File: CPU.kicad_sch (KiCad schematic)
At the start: 215 parts, among them J1 Conn_02x36_Top_Bottom, P10 Conn_02x08_Counter_Clockwise, P2 Conn_02x13_Top_Bottom, P3 Conn_02x13_Top_Bottom, P4 Conn_02x08_Counter_Clockwise, P5 Conn_02x25_Counter_Clockwise, P6 Conn_02x25_Counter_Clockwise, P7 Conn_02x07_Counter_Clockwise, P8 Conn_02x08_Counter_Clockwise

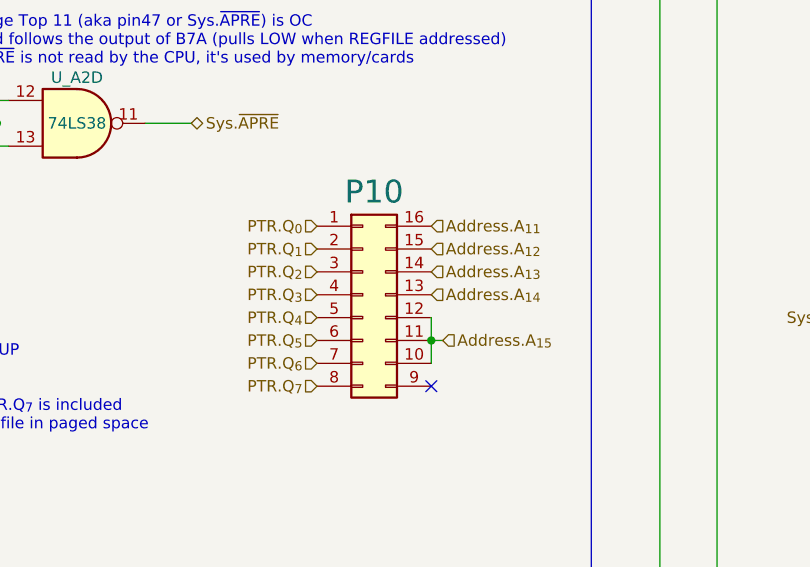
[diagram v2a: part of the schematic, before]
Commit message: Remove P10
This diagnostics connector gives direct access to page table DRAM, we don't need
it. In fact it could have been located in B row with much shorter traces, but
the only available position there is occupied by second ISA ROM half.
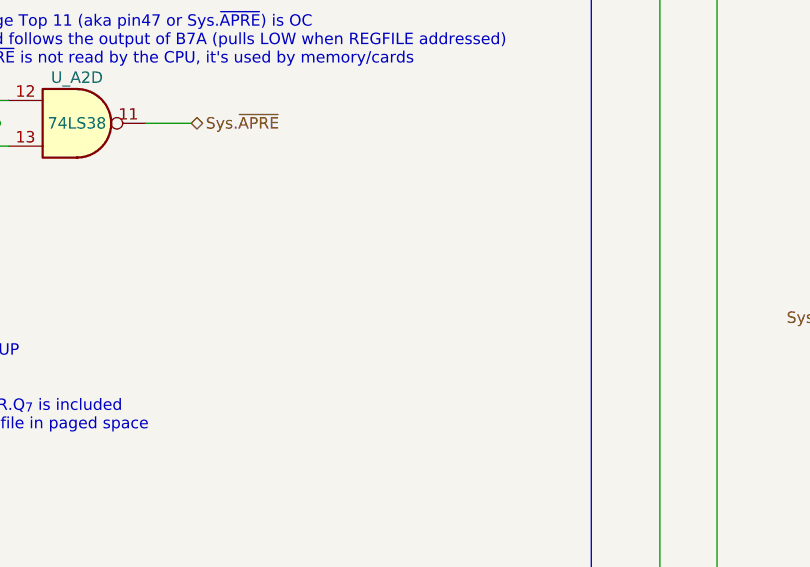
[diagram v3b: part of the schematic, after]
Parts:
- removed P10: Conn_02x08_Counter_Clockwise, Package_DIP:DIP-16_W7.62mm_Socket, symbol Connector_Generic:Conn_02x08_Counter_Clockwise
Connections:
- no-connect marks 94 -> 93
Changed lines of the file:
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@@
   (junction (at 107.95 429.26) (diameter 0) (color 0 0 0 0)
   )
-  (junction (at 341.63 494.03) (diameter 0) (color 0 0 0 0)
-  )
   (junction (at 144.78 457.2) (diameter 0) (color 0 0 0 0)
   )
@@
   (no_connect (at 440.69 746.76))
   (no_connect (at 289.56 142.24))
-  (no_connect (at 341.63 499.11))
   (no_connect (at 386.08 356.87))
   (no_connect (at 521.97 367.03))
@@
     (stroke (width 0) (type default) (color 189 121 184 1))
   )
-  (wire (pts (xy 341.63 491.49) (xy 341.63 494.03))
-    (stroke (width 0) (type default) (color 0 0 0 0))
-  )
   (wire (pts (xy 871.22 123.19) (xy 875.03 123.19))
     (stroke (width 0) (type default) (color 0 0 0 0))
@@
     (stroke (width 0) (type default) (color 0 0 0 0))
   )
-  (wire (pts (xy 341.63 494.03) (xy 341.63 496.57))
-    (stroke (width 0) (type default) (color 0 0 0 0))
-  )
   (wire (pts (xy 615.95 748.03) (xy 615.95 758.19))
     (stroke (width 0) (type default) (color 0 0 0 0))
@@
     (stroke (width 0) (type default) (color 0 0 0 0))
   )
-  (wire (pts (xy 342.9 494.03) (xy 341.63 494.03))
-    (stroke (width 0) (type default) (color 0 0 0 0))
-  )
   (wire (pts (xy 864.87 245.11) (xy 886.46 245.11))
     (stroke (width 0) (type default) (color 0 0 0 0))
@@
     (effects (font (size 1.27 1.27)) (justify right))
   )
-  (hierarchical_label "PTR.Q_{7}" (shape input) (at 328.93 499.11 180)
-    (effects (font (size 1.27 1.27)) (justify right))
-  )
   (hierarchical_label "~{M13_EN}" (shape output) (at 674.37 142.24 0)
     (effects (font (size 1.27 1.27)) (justify left))
@@
     (effects (font (size 1.27 1.27)) (justify right))
   )
-  (hierarchical_label "Address.A_{15}" (shape input) (at 342.9 494.03 0)
-    (effects (font (size 1.27 1.27)) (justify left))
-  )
   (hierarchical_label "CondRegOrPageOut" (shape output) (at 300.99 454.66 0)
     (effects (font (size 1.27 1.27)) (justify left))
@@
     (effects (font (size 1.27 1.27)) (justify right))
   )
-  (hierarchical_label "Address.A_{14}" (shape input) (at 341.63 488.95 0)
-    (effects (font (size 1.27 1.27)) (justify left))
-  )
   (hierarchical_label "~{M13_EN}" (shape input) (at 985.52 270.51 180)
     (effects (font (size 1.27 1.27)) (justify right))
@@
     (effects (font (size 1.27 1.27)) (justify left))
   )
-  (hierarchical_label "PTR.Q_{6}" (shape input) (at 328.93 496.57 180)
-    (effects (font (size 1.27 1.27)) (justify right))
-  )
   (hierarchical_label "~{AddrMToData}" (shape input) (at 109.22 472.44 180)
     (effects (font (size 1.27 1.27)) (justify right))
@@
     (effects (font (size 1.27 1.27)) (justify left))
   )
-  (hierarchical_label "Address.A_{13}" (shape input) (at 341.63 486.41 0)
-    (effects (font (size 1.27 1.27)) (justify left))
-  )
   (hierarchical_label "DMA.~{INTRequest}" (shape input) (at 909.32 250.19 180)
     (effects (font (size 1.27 1.27)) (justify right))
@@
     (effects (font (size 1.27 1.27)) (justify left))
   )
-  (hierarchical_label "Address.A_{12}" (shape input) (at 341.63 483.87 0)
-    (effects (font (size 1.27 1.27)) (justify left))
-  )
   (hierarchical_label "~{WorkAddr_LD_LO}" (shape output) (at 674.37 152.4 0)
     (effects (font (size 1.27 1.27)) (justify left))
@@
     (effects (font (size 1.27 1.27)) (justify left))
   )
-  (hierarchical_label "PTR.Q_{1}" (shape input) (at 328.93 483.87 180)
-    (effects (font (size 1.27 1.27)) (justify right))
-  )
   (hierarchical_label "Sys.~{A_{9}}" (shape bidirectional) (at 41.91 408.94 180)
     (effects (font (size 1.27 1.27)) (justify right))
@@
     (effects (font (size 1.27 1.27)) (justify right))
   )
-  (hierarchical_label "Address.A_{11}" (shape input) (at 341.63 481.33 0)
-    (effects (font (size 1.27 1.27)) (justify left))
-  )
   (hierarchical_label "MWR.A6_{3}" (shape input) (at 740.41 798.83 90)
     (effects (font (size 1.27 1.27)) (justify left))
@@
     (effects (font (size 1.27 1.27)) (justify left))
   )
-  (hierarchical_label "PTR.Q_{2}" (shape input) (at 328.93 486.41 180)
-    (effects (font (size 1.27 1.27)) (justify right))
-  )
   (hierarchical_label "~{Swap_OE}" (shape output) (at 466.09 623.57 0)
     (effects (font (size 1.27 1.27)) (justify left))
@@
     (effects (font (size 1.27 1.27)) (justify right))
   )
-  (hierarchical_label "PTR.Q_{5}" (shape input) (at 328.93 494.03 180)
-    (effects (font (size 1.27 1.27)) (justify right))
-  )
   (hierarchical_label "MWR.F1_{5}" (shape input) (at 618.49 798.83 90)
     (effects (font (size 1.27 1.27)) (justify left))
@@
     (effects (font (size 1.27 1.27)) (justify left))
   )
-  (hierarchical_label "PTR.Q_{0}" (shape input) (at 328.93 481.33 180)
-    (effects (font (size 1.27 1.27)) (justify right))
-  )
   (hierarchical_label "Sys.~{INTREQ}" (shape input) (at 720.09 101.6 180)
     (effects (font (size 1.27 1.27)) (justify right))
@@
     (effects (font (size 1.27 1.27)) (justify left))
   )
-  (hierarchical_label "PTR.Q_{4}" (shape input) (at 328.93 491.49 180)
-    (effects (font (size 1.27 1.27)) (justify right))
-  )
   (hierarchical_label "M10C_a" (shape output) (at 450.85 262.89 0)
     (effects (font (size 1.27 1.27)) (justify left))
@@
     (effects (font (size 1.27 1.27)) (justify right))
   )
-  (hierarchical_label "PTR.Q_{3}" (shape input) (at 328.93 488.95 180)
-    (effects (font (size 1.27 1.27)) (justify right))
-  )
   (hierarchical_label "Sys.~{CPL_{2}}" (shape bidirectional) (at 100.33 397.51 180)
     (effects (font (size 1.27 1.27)) (justify right))
@@
     (pin "9")
   )
-  (symbol (lib_id "Connector_Generic:Conn_02x08_Counter_Clockwise") (at 334.01 488.95 0) (unit 1)
-    (in_bom yes) (on_board yes)
-    (property "Reference" "P10" (id 0) (at 335.28 477.52 0)
-      (effects (font (size 2.54 2.54)))
-    )
-    (property "Value" "Conn_02x08_Counter_Clockwise" (id 1) (at 335.28 477.52 0)
-      (effects (font (size 1.27 1.27)) hide)
-    )
-    (property "Footprint" "Package_DIP:DIP-16_W7.62mm_Socket" (id 2) (at 334.01 488.95 0)
-      (effects (font (size 1.27 1.27)) hide)
-    )
-    (property "Datasheet" "~" (id 3) (at 334.01 488.95 0)
-      (effects (font (size 1.27 1.27)) hide)
-    )
-    (pin "1")
-    (pin "10")
-    (pin "11")
-    (pin "12")
-    (pin "13")
-    (pin "14")
-    (pin "15")
-    (pin "16")
-    (pin "2")
-    (pin "3")
-    (pin "4")
-    (pin "5")
-    (pin "6")
-    (pin "7")
-    (pin "8")
-    (pin "9")
-  )
   (symbol (lib_id "74xx:74LS74") (at 684.53 41.91 0) (unit 3)
     (in_bom yes) (on_board yes)
@@
       (reference "P8") (unit 1) (value "Conn_02x08_Counter_Clockwise") (footprint "Package_DIP:DIP-16_W7.62mm_Socket")
     )
-    (path "/5526b978-6091-4308-8cc5-df61e46dff5e"
-      (reference "P10") (unit 1) (value "Conn_02x08_Counter_Clockwise") (footprint "Package_DIP:DIP-16_W7.62mm_Socket")
-    )
     (path "/314bd753-a531-42e2-88ae-163e7747a0c2"

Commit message: Fixed U13H/U13L footprint
Noticed in time and replaced with proper DIP16 instead of DIP20, erroneously
left over from the original ROM
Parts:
- U_BH13, U_BL13: footprint Package_DIP:DIP-20_W7.62mm -> Package_DIP:DIP-16_W7.62mm
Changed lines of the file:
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@@
     )
     (property "Value" "93427C" (id 1) (at 224.79 54.61 90))
-    (property "Footprint" "Package_DIP:DIP-20_W7.62mm" (id 2) (at 247.65 29.21 0)
+    (property "Footprint" "Package_DIP:DIP-16_W7.62mm" (id 2) (at 247.65 29.21 0)
       (effects (font (size 1.27 1.27)) hide)
     )
@@
     )
     (property "Value" "93427C" (id 1) (at 224.79 97.79 90))
-    (property "Footprint" "Package_DIP:DIP-20_W7.62mm" (id 2) (at 247.65 72.39 0)
+    (property "Footprint" "Package_DIP:DIP-16_W7.62mm" (id 2) (at 247.65 72.39 0)
       (effects (font (size 1.27 1.27)) hide)
     )
@@
     )
     (path "/c0266c95-ae17-45e2-bf80-9f2f693576d4"
-      (reference "U_BH13") (unit 1) (value "93427C") (footprint "Package_DIP:DIP-20_W7.62mm")
+      (reference "U_BH13") (unit 1) (value "93427C") (footprint "Package_DIP:DIP-16_W7.62mm")
     )
     (path "/87f1dd62-191b-408d-8ad7-44a75dff6333"
-      (reference "U_BL13") (unit 1) (value "93427C") (footprint "Package_DIP:DIP-20_W7.62mm")
+      (reference "U_BL13") (unit 1) (value "93427C") (footprint "Package_DIP:DIP-16_W7.62mm")
     )
     (path "/8af415d4-268f-42b0-9c51-01a0acd645d3"

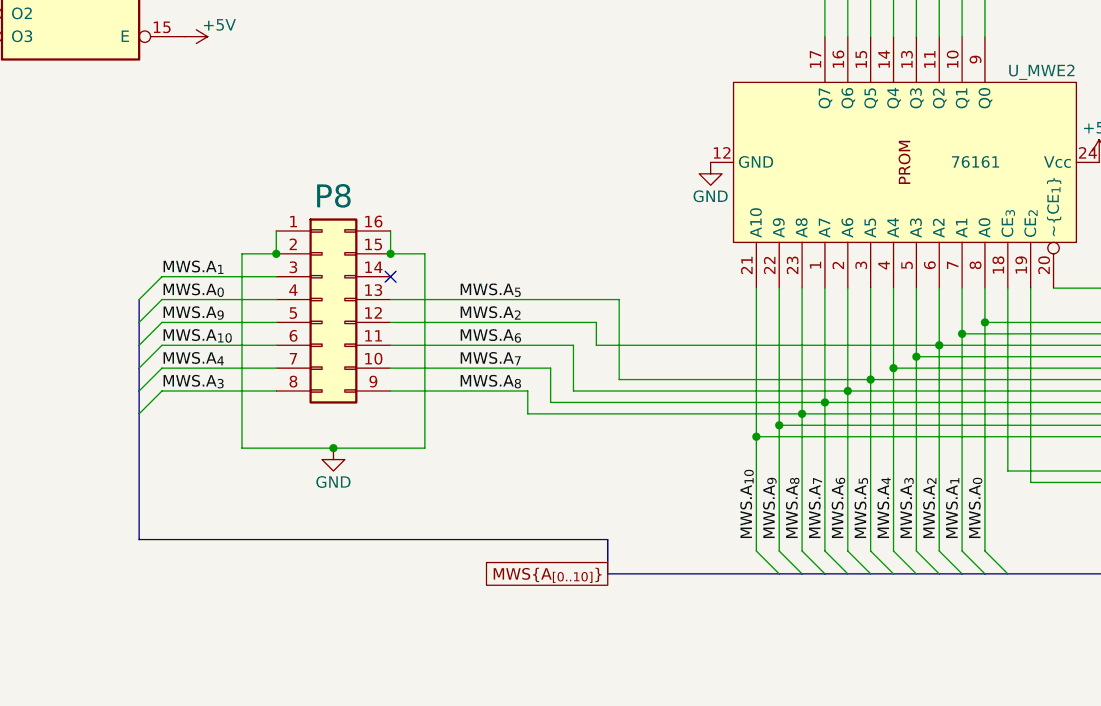
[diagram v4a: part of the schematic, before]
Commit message: P8 pins reassigned
Change connector type to IDC for smaller footprint and rearrange pins so that
less vias are needed.

All the footprints brought in sync with the PCB
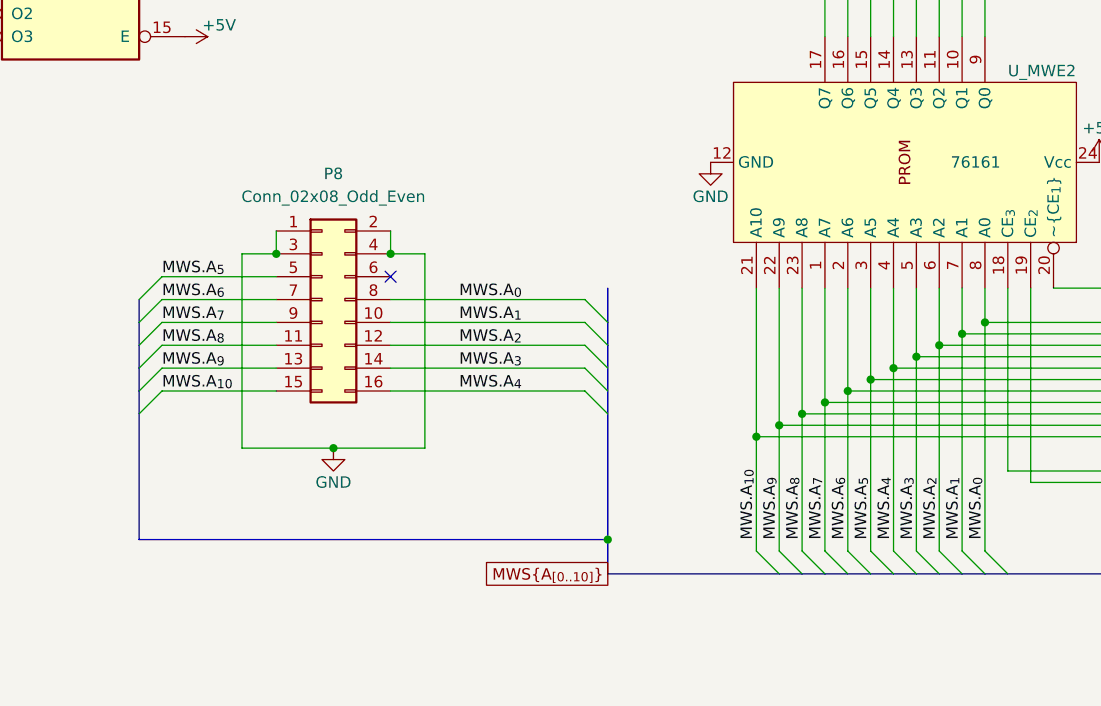
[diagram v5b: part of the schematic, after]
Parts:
- removed P8: Conn_02x08_Counter_Clockwise, Package_DIP:DIP-16_W7.62mm_Socket, symbol Connector_Generic:Conn_02x08_Counter_Clockwise
- added P8: Conn_02x08_Odd_Even, Connector_IDC:IDC-Header_2x08_P2.54mm_Vertical, symbol Connector_Generic:Conn_02x08_Odd_Even
- C31, C32, C33, C34, C35: footprint Capacitor_THT:C_Disc_D4.3mm_W1.9mm_P5.00mm -> Capacitor_THT:C_Rect_L9.0mm_W2.5mm_P7.50mm_MKT
- C52, C53: footprint Capacitor_THT:CP_Axial_L25.0mm_D10.0mm_P30.00mm_Horizontal -> Capacitor_THT:CP_Radial_D8.0mm_P3.50mm
- R18: footprint Resistor_THT:R_Axial_DIN0207_L6.3mm_D2.5mm_P10.16mm_Horizontal -> Resistor_THT:R_Axial_DIN0207_L6.3mm_D2.5mm_P7.62mm_Horizontal
- R19: footprint Resistor_THT:R_Axial_DIN0207_L6.3mm_D2.5mm_P10.16mm_Horizontal -> Resistor_THT:R_Axial_DIN0204_L3.6mm_D1.6mm_P7.62mm_Horizontal
- R22, R23: footprint Resistor_THT:R_Axial_DIN0204_L3.6mm_D1.6mm_P2.54mm_Vertical -> Resistor_THT:R_Axial_DIN0204_L3.6mm_D1.6mm_P5.08mm_Horizontal
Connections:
- net GND: now also P8.1 (Pin_1), P8.2 (Pin_2), P8.3 (Pin_3), P8.4 (Pin_4)
- net MWS.A_{0}: now also P8.8 (Pin_8)
- net MWS.A_{10}: now also P8.15 (Pin_15)
- net MWS.A_{1}: now also P8.10 (Pin_10)
- net MWS.A_{2}: now also P8.12 (Pin_12)
- net MWS.A_{3}: now also P8.14 (Pin_14)
- net MWS.A_{4}: now also P8.16 (Pin_16)
- net MWS.A_{5}: now also P8.5 (Pin_5)
- net MWS.A_{6}: now also P8.7 (Pin_7)
- net MWS.A_{7}: now also P8.9 (Pin_9)
- net MWS.A_{8}: now also P8.11 (Pin_11)
- net MWS.A_{9}: now also P8.13 (Pin_13)
